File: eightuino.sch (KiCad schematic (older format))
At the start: 23 parts, among them CON1 BARREL_JACK, IC1 ATMEGA8-P, P1 PowerPins, P2 Analog, P3 Digital1, P4 Digital_2, P5 Serial, P6 ISP, SW1 SW_PUSH_SMALL, U1 NCP1117ST33T3G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

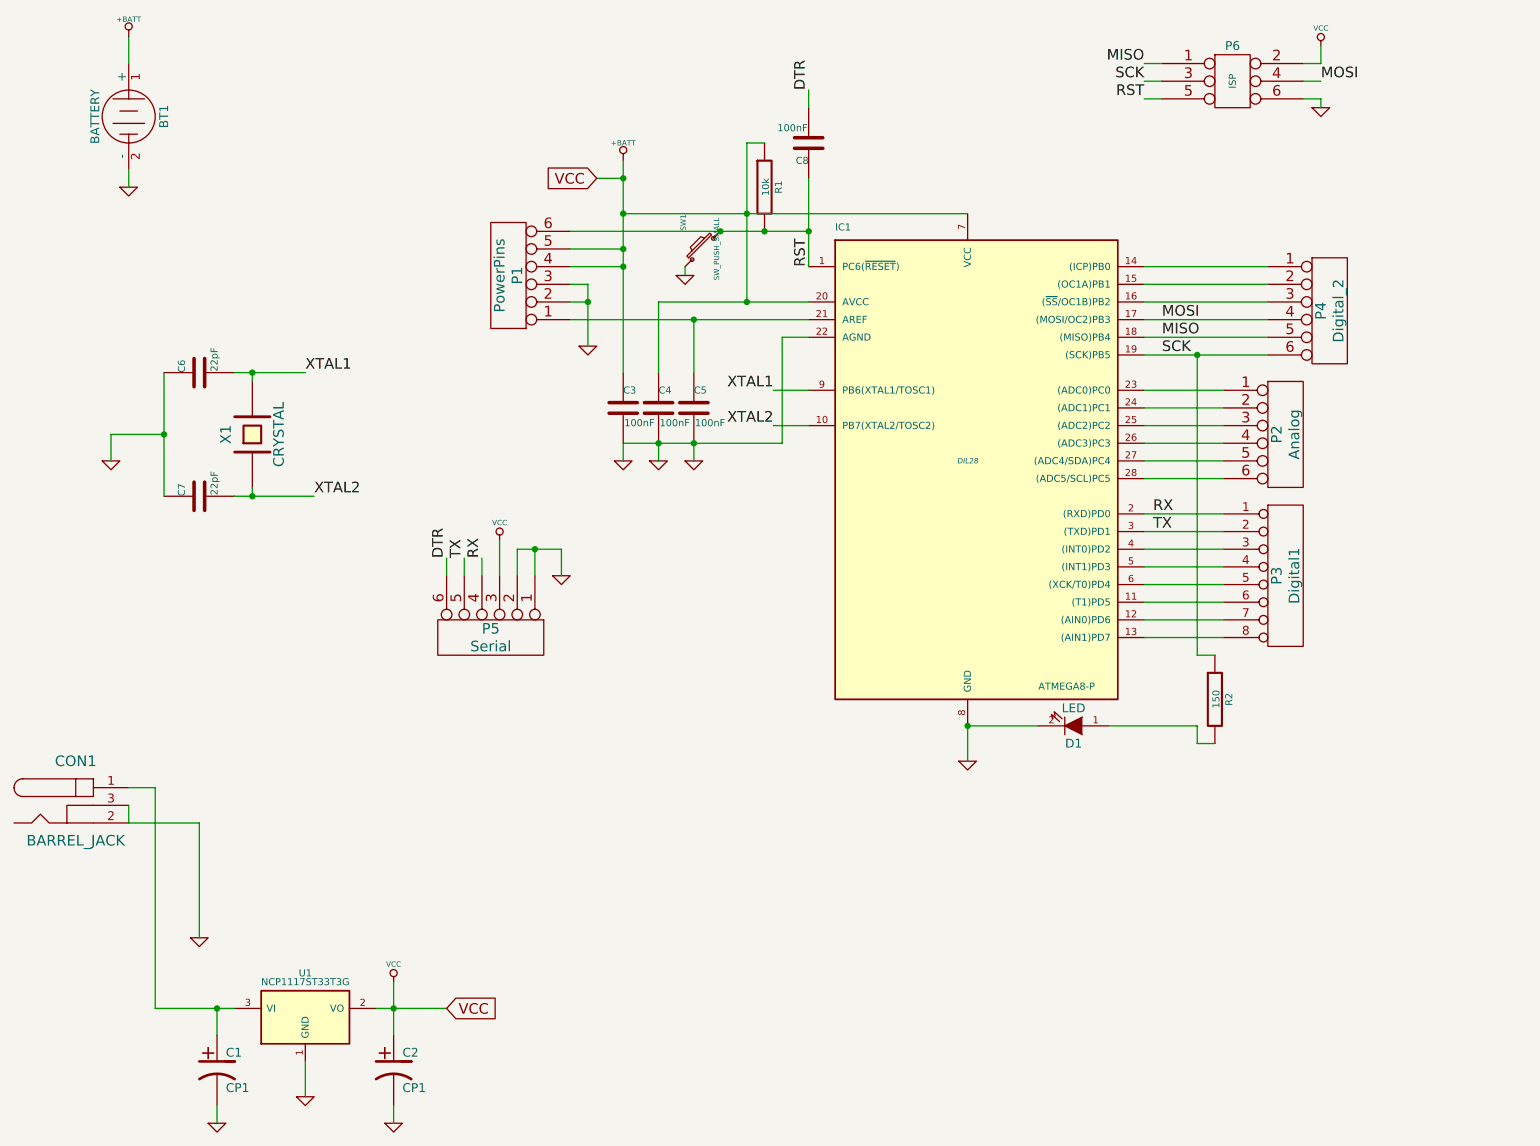
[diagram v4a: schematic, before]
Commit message: Changed to tfqp32 package and added ADC6 and ADC7
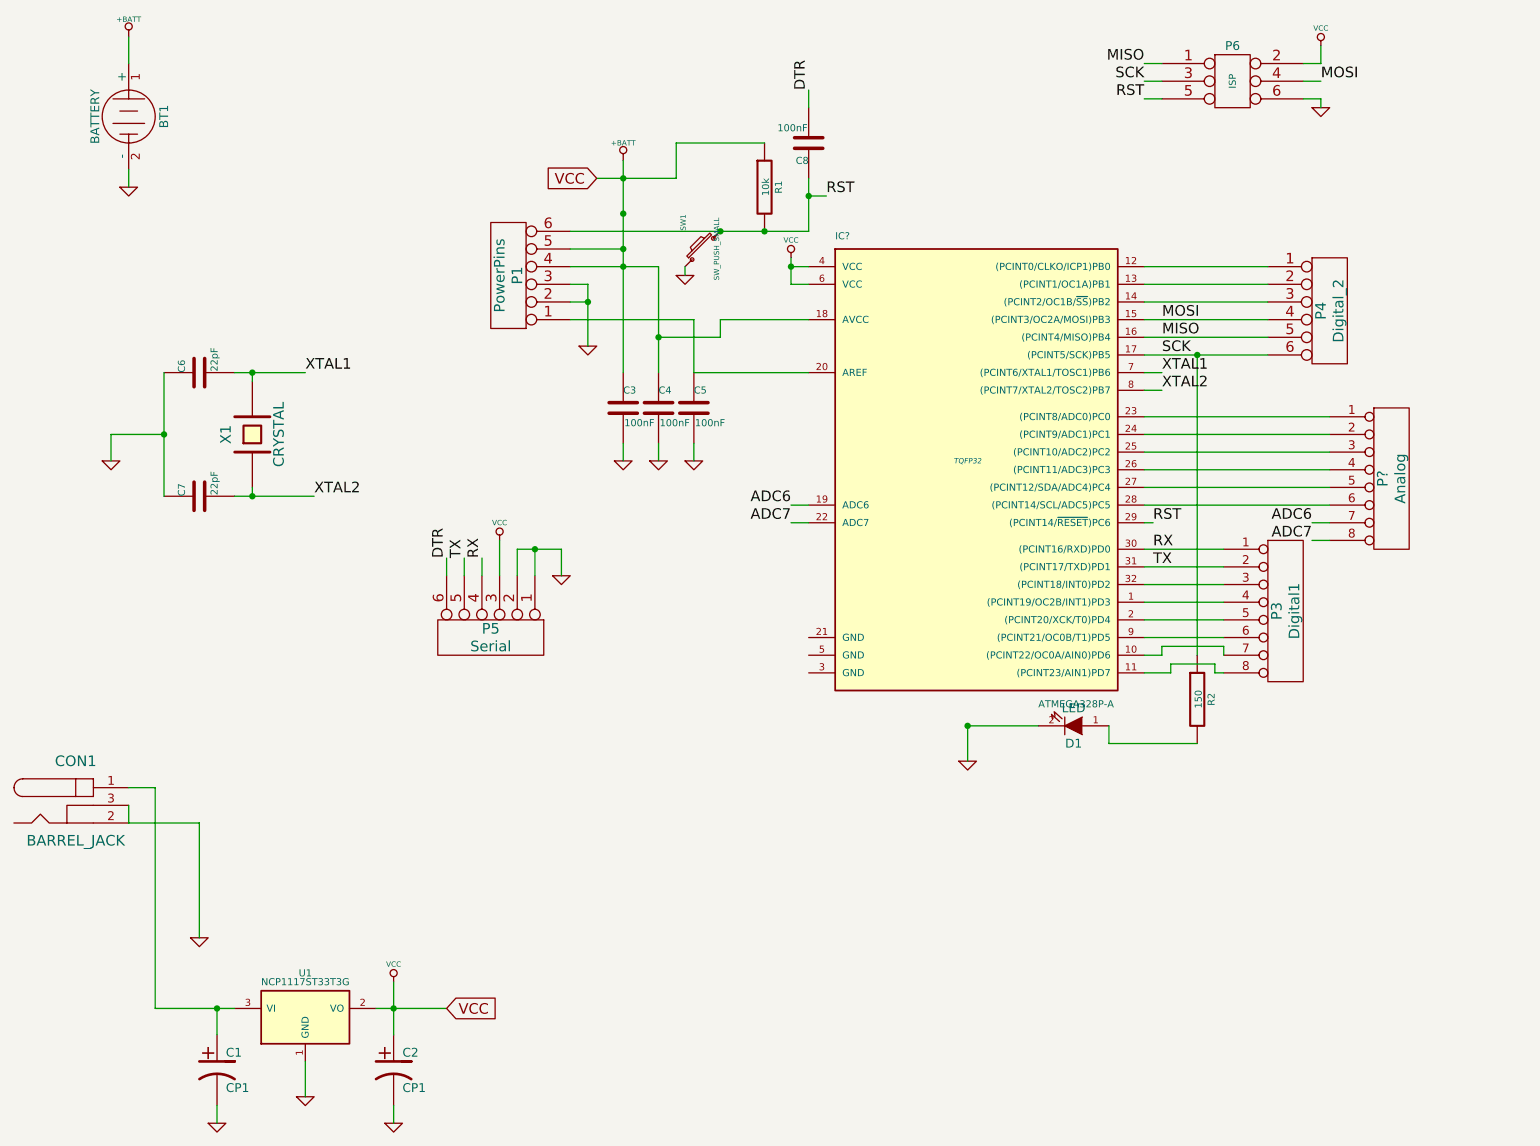
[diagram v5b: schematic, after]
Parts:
- removed IC1: ATMEGA8-P, DIL28, symbol ATMEGA8-P
- removed P2: Analog, ~, symbol CONN_6
- added IC?: ATMEGA328P-A, TQFP32, symbol ATMEGA328P-A
- added P?: Analog, symbol CONN_8
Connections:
- net +BATT: now also IC?.18 (AVCC), IC?.4 (VCC), IC?.6 (VCC)
- net MISO: now also IC?.16 ((PCINT4/MISO)PB4)
- net MOSI: now also IC?.15 ((PCINT3/OC2A/MOSI)PB3)
- net RST: now also IC?.29 ((PCINT14/~RESET~)PC6)
- net RX: now also IC?.30 ((PCINT16/RXD)PD0)
- net SCK: now also IC?.17 ((PCINT5/SCK)PB5)
- net TX: now also IC?.31 ((PCINT17/TXD)PD1)
- net XTAL1: now also IC?.7 ((PCINT6/XTAL1/TOSC1)PB6)
- net XTAL2: now also IC?.8 ((PCINT7/XTAL2/TOSC2)PB7)
- net at P3.6 (P6): now also IC?.9 ((PCINT21/OC0B/T1)PD5)
- net at P3.7 (P7): now also IC?.10 ((PCINT22/OC0A/AIN0)PD6)
- net at P3.8 (P8): now also IC?.11 ((PCINT23/AIN1)PD7)
- net at P4.1: now also IC?.12 ((PCINT0/CLKO/ICP1)PB0)
- net at P4.2: now also IC?.13 ((PCINT1/OC1A)PB1)
- net at P4.3: now also IC?.14 ((PCINT2/OC1B/~SS~)PB2)
- net at C5.1, P1.1: now also IC?.20 (AREF)
- net at P3.3 (P3): now also IC?.32 ((PCINT18/INT0)PD2)
- net at P3.4 (P4): now also IC?.1 ((PCINT19/OC2B/INT1)PD3)
- net at P3.5 (P5): now also IC?.2 ((PCINT20/XCK/T0)PD4)
- new net: IC?.23 ((PCINT8/ADC0)PC0), P?.1 (P1)
- new net: IC?.24 ((PCINT9/ADC1)PC1), P?.2 (P2)
- new net: IC?.25 ((PCINT10/ADC2)PC2), P?.3 (P3)
- new net: IC?.26 ((PCINT11/ADC3)PC3), P?.4 (P4)
- new net: IC?.27 ((PCINT12/SDA/ADC4)PC4), P?.5 (P5)
- new net: IC?.28 ((PCINT14/SCL/ADC5)PC5), P?.6 (P6)
- new net ADC6: IC?.19 (ADC6), P?.7 (P7)
- new net ADC7: IC?.22 (ADC7), P?.8 (P8)
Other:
- moved on the sheet: P3, R2
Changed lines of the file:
@@
 $EndDescr
-$Comp
-L CONN_6 P2
-U 1 1 528CF788
-P 8650 3150
-F 0 "P2" V 8600 3150 60  0000 C CNN
-F 1 "Analog" V 8700 3150 60  0000 C CNN
-F 2 "~" H 8650 3150 60  0000 C CNN
-F 3 "~" H 8650 3150 60  0000 C CNN
-	1    8650 3150
-	1    0    0    -1
-$EndComp
 $Comp
 L CONN_6 P4
@@
 L CONN_8 P3
 U 1 1 528CF85A
-P 8650 3950
-F 0 "P3" V 8600 3950 60  0000 C CNN
-F 1 "Digital1" V 8700 3950 60  0000 C CNN
-F 2 "~" H 8650 3950 60  0000 C CNN
-F 3 "~" H 8650 3950 60  0000 C CNN
-	1    8650 3950
+P 8650 4150
+F 0 "P3" V 8600 4150 60  0000 C CNN
+F 1 "Digital1" V 8700 4150 60  0000 C CNN
+F 2 "~" H 8650 4150 60  0000 C CNN
+F 3 "~" H 8650 4150 60  0000 C CNN
+	1    8650 4150
 	1    0    0    -1
 $EndComp
@@
 $EndComp
 $Comp
-L ATMEGA8-P IC1
-U 1 1 528CF67E
-P 6850 3300
-F 0 "IC1" H 6100 4600 40  0000 L BNN
-F 1 "ATMEGA8-P" H 7250 2000 40  0000 L BNN
-F 2 "DIL28" H 6850 3300 30  0000 C CIN
-F 3 "" H 6850 3300 60  0000 C CNN
-	1    6850 3300
-	1    0    0    -1
-$EndComp
-$Comp
 L C C3
 U 1 1 528D0B0F
@@
 L R R2
 U 1 1 52926621
-P 8250 4650
-F 0 "R2" V 8330 4650 40  0000 C CNN
-F 1 "150" V 8257 4651 40  0000 C CNN
-F 2 "~" V 8180 4650 30  0000 C CNN
-F 3 "~" H 8250 4650 30  0000 C CNN
-	1    8250 4650
+P 8150 4650
+F 0 "R2" V 8230 4650 40  0000 C CNN
+F 1 "150" V 8157 4651 40  0000 C CNN
+F 2 "~" V 8080 4650 30  0000 C CNN
+F 3 "~" H 8150 4650 30  0000 C CNN
+	1    8150 4650
 	1    0    0    -1
 $EndComp
@@
 	1    0    0    -1
 $EndComp
-Text Label 5750 2900 2    60   ~ 0
+Text Label 7950 2800 0    60   ~ 0
 XTAL1
-Text Label 5750 3100 2    60   ~ 0
+Text Label 7950 2900 0    60   ~ 0
 XTAL2
 $Comp
@@
 Text Label 5950 1200 1    60   ~ 0
 DTR
-Text Label 7900 3600 0    60   ~ 0
+Text Label 7900 3800 0    60   ~ 0
 RX
-Text Label 7900 3700 0    60   ~ 0
+Text Label 7900 3900 0    60   ~ 0
 TX
 $Comp
@@
 Text Label 7950 2700 0    60   ~ 0
 SCK
-Text Label 5950 2200 1    60   ~ 0
+Text Label 6050 1800 0    60   ~ 0
 RST
 $Comp
@@
 	6850 4800 6850 5000
 Wire Wire Line
-	5800 3200 5800 2600
-Wire Wire Line
-	5950 1700 5950 2200
-Wire Wire Line
 	5950 1200 5950 1300
 Wire Wire Line
@@
 	2300 3500 2300 2800
 Wire Wire Line
-	5750 3100 5950 3100
-Wire Wire Line
-	5750 2900 5950 2900
-Wire Wire Line
 	2100 1050 2100 900
 Connection ~ 4900 1700
@@
 Wire Wire Line
 	2500 5350 2100 5350
-Wire Wire Line
-	8150 4900 8250 4900
-Wire Wire Line
-	8150 4800 8150 4900
-Wire Wire Line
-	8150 4400 8250 4400
 Connection ~ 3600 6400
 Connection ~ 4900 1900
 Wire Wire Line
-	4750 1700 4900 1700
-Wire Wire Line
-	5800 2600 5950 2600
+	4750 1700 5200 1700
 Connection ~ 2600 6400
 Wire Wire Line
@@
 	2500 5350 2500 6000
 Connection ~ 6850 4800
-Wire Wire Line
-	7650 4800 8150 4800
 Connection ~ 8150 2700
-Connection ~ 5950 2000
 Connection ~ 5700 2000
 Wire Wire Line
-	4600 2000 5950 2000
-Wire Wire Line
-	5600 1500 5700 1500
+	5200 1500 5700 1500
 Connection ~ 5450 2000
 Wire Wire Line
@@
 Connection ~ 4900 2200
 Wire Wire Line
-	4900 2200 4600 2200
+	4600 2200 5100 2200
 Connection ~ 4700 2400
 Wire Wire Line
 	4700 2300 4600 2300
-Connection ~ 5600 2400
-Connection ~ 5300 2500
 Wire Wire Line
 	4700 2300 4700 2650
 Wire Wire Line
 	4600 2400 4700 2400
-Connection ~ 5600 1900
 Wire Wire Line
 	4900 1600 4900 2800
 Wire Wire Line
-	5100 2400 5100 2800
-Wire Wire Line
-	5950 2400 5100 2400
+	5100 2200 5100 2800
 Wire Wire Line
 	5300 2500 5300 2800
-Connection ~ 5100 3200
-Connection ~ 5300 3200
-Wire Wire Line
-	4900 3200 5800 3200
 Wire Wire Line
 	4900 3200 4900 3300
@@
 	5300 3200 5300 3300
 Wire Wire Line
-	4600 2500 5950 2500
-Wire Wire Line
-	5600 1500 5600 2400
-Wire Wire Line
 	8550 2200 7850 2200
 Wire Wire Line
@@
 Wire Wire Line
 	8300 3800 7850 3800
-Wire Wire Line
-	8300 3700 7850 3700
-Wire Wire Line
-	8300 3600 7850 3600
-Wire Wire Line
-	8300 3400 7850 3400
-Wire Wire Line
-	8300 3300 7850 3300
-Wire Wire Line
-	8300 3200 7850 3200
-Wire Wire Line
-	8300 3100 7850 3100
-Wire Wire Line
-	8300 3000 7850 3000
-Wire Wire Line
-	8300 2900 7850 2900
-Wire Wire Line
-	4900 1900 6850 1900
 Wire Wire Line
 	2250 6400 2700 6400
@@
 	1    0    0    -1
 $EndComp
+Wire Wire Line
+	8300 4400 8300 4350
+Wire Wire Line
+	8300 4350 7950 4350
+Wire Wire Line
+	7950 4350 7950 4400
+Wire Wire Line
+	7950 4400 7850 4400
+Wire Wire Line
+	8150 4900 7650 4900
+Wire Wire Line
+	7650 4900 7650 4800
+Wire Wire Line
+	8300 4500 8250 4500
+Wire Wire Line
+	8250 4500 8250 4450
+Wire Wire Line
+	8250 4450 8000 4450
+Wire Wire Line
+	8000 4450 8000 4500
+Wire Wire Line
+	8000 4500 7850 4500
+Wire Wire Line
+	7850 3050 8900 3050
+Wire Wire Line
+	7850 3150 8900 3150
+Wire Wire Line
+	7850 3250 8900 3250
+Wire Wire Line
+	7850 3350 8900 3350
+Wire Wire Line
+	7850 3450 8900 3450
+Wire Wire Line
+	7850 3550 8900 3550
+Wire Wire Line
+	6050 1800 5950 1800
+Connection ~ 5950 1800
+Wire Wire Line
+	5950 2000 4600 2000
+Wire Wire Line
+	5950 1700 5950 2000
+Wire Wire Line
+	7950 2800 7850 2800
+Wire Wire Line
+	7950 2900 7850 2900
+Text Label 7900 3650 0    60   ~ 0
+RST
+Wire Wire Line
+	7900 3650 7850 3650
+Wire Wire Line
+	5300 2800 5950 2800
+Wire Wire Line
+	5300 2500 4600 2500
+$Comp
+L ATMEGA328P-A IC?
+U 1 1 52E2E72B
+P 6850 3300
+F 0 "IC?" H 6100 4550 40  0000 L BNN
+F 1 "ATMEGA328P-A" H 7250 1900 40  0000 L BNN
+F 2 "TQFP32" H 6850 3300 30  0000 C CIN
+F 3 "" H 6850 3300 60  0000 C CNN
+	1    6850 3300
+	1    0    0    -1
+$EndComp
+Wire Wire Line
+	5950 2500 5450 2500
+Wire Wire Line
+	5450 2500 5450 2600
+Wire Wire Line
+	5450 2600 5100 2600
+Connection ~ 5100 2600
+Wire Wire Line
+	5200 1700 5200 1500
+$Comp
+L VCC #PWR?
+U 1 1 52E2F21D
+P 5850 2150
+F 0 "#PWR?" H 5850 2250 30  0001 C CNN
+F 1 "VCC" H 5850 2250 30  0000 C CNN
+F 2 "" H 5850 2150 60  0000 C CNN
+F 3 "" H 5850 2150 60  0000 C CNN
+	1    5850 2150
+	1    0    0    -1
+$EndComp
+Wire Wire Line
+	5950 2200 5850 2200
+Wire Wire Line
+	5850 2150 5850 2300
+Wire Wire Line
+	5850 2300 5950 2300
+Connection ~ 5850 2200
+$Comp
+L CONN_8 P?
+U 1 1 52E2F32E
+P 9250 3400
+F 0 "P?" V 9200 3400 60  0000 C CNN
+F 1 "Analog" V 9300 3400 60  0000 C CNN
+F 2 "" H 9250 3400 60  0000 C CNN
+F 3 "" H 9250 3400 60  0000 C CNN
+	1    9250 3400
+	1    0    0    -1
+$EndComp
+Text Label 8800 3650 2    60   ~ 0
+ADC6
+Text Label 8800 3750 2    60   ~ 0
+ADC7
+Wire Wire Line
+	8900 3750 8800 3750
+Wire Wire Line
+	8900 3650 8800 3650
+Text Label 5850 3550 2    60   ~ 0
+ADC6
+Text Label 5850 3650 2    60   ~ 0
+ADC7
+Wire Wire Line
+	5950 3550 5850 3550
+Wire Wire Line
+	5950 3650 5850 3650
 $EndSCHEMATC
